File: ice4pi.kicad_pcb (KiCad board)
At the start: 4 copper layers, 85 x 56 mm, 40 parts, among them J1 Conn_02x03, J2 Raspberry_Pi_2_3, J3 USB_C_Receptacle_USB2.0, J4 RJ45_Abracon_ARJP11A-MASA-B-A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, U1 ENC28J60x-SS, U2 DSC1001DE1-025.0000, U3 TPS2375-1

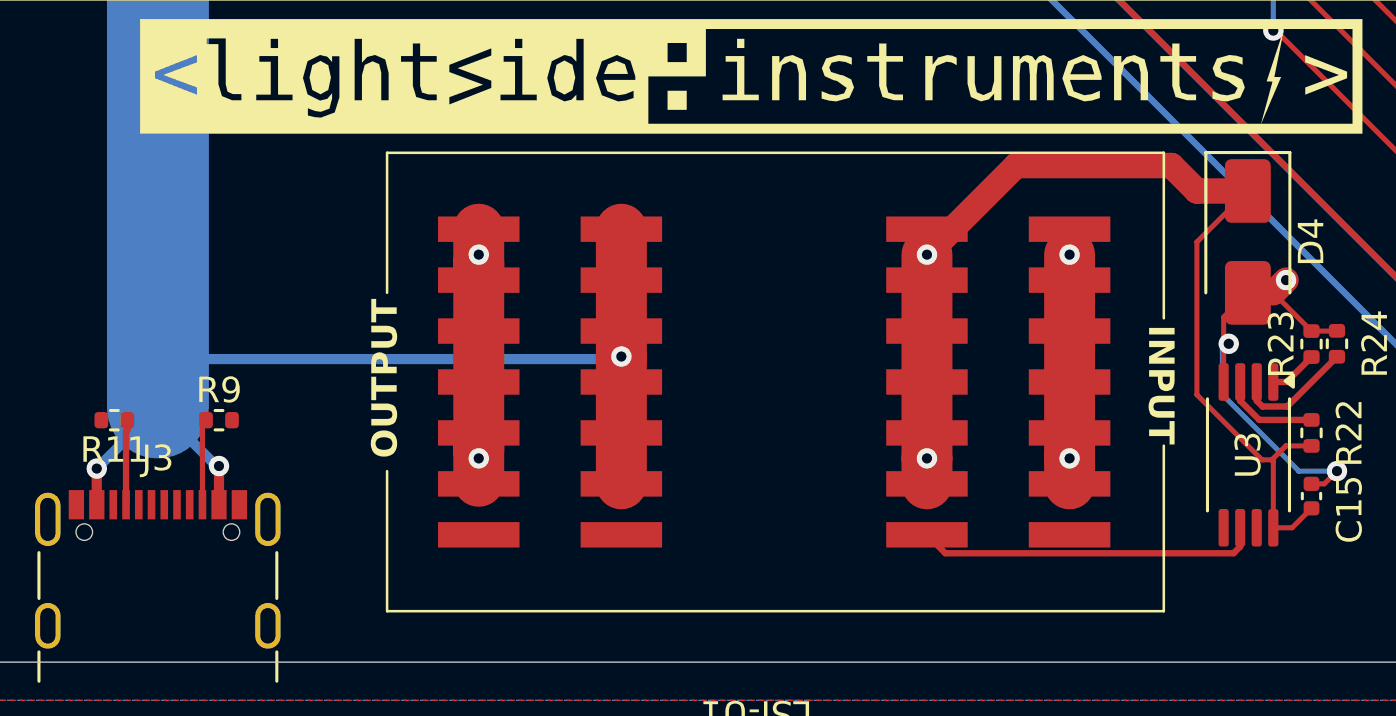
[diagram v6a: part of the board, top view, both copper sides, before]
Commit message: fix: fixed powermod footprint
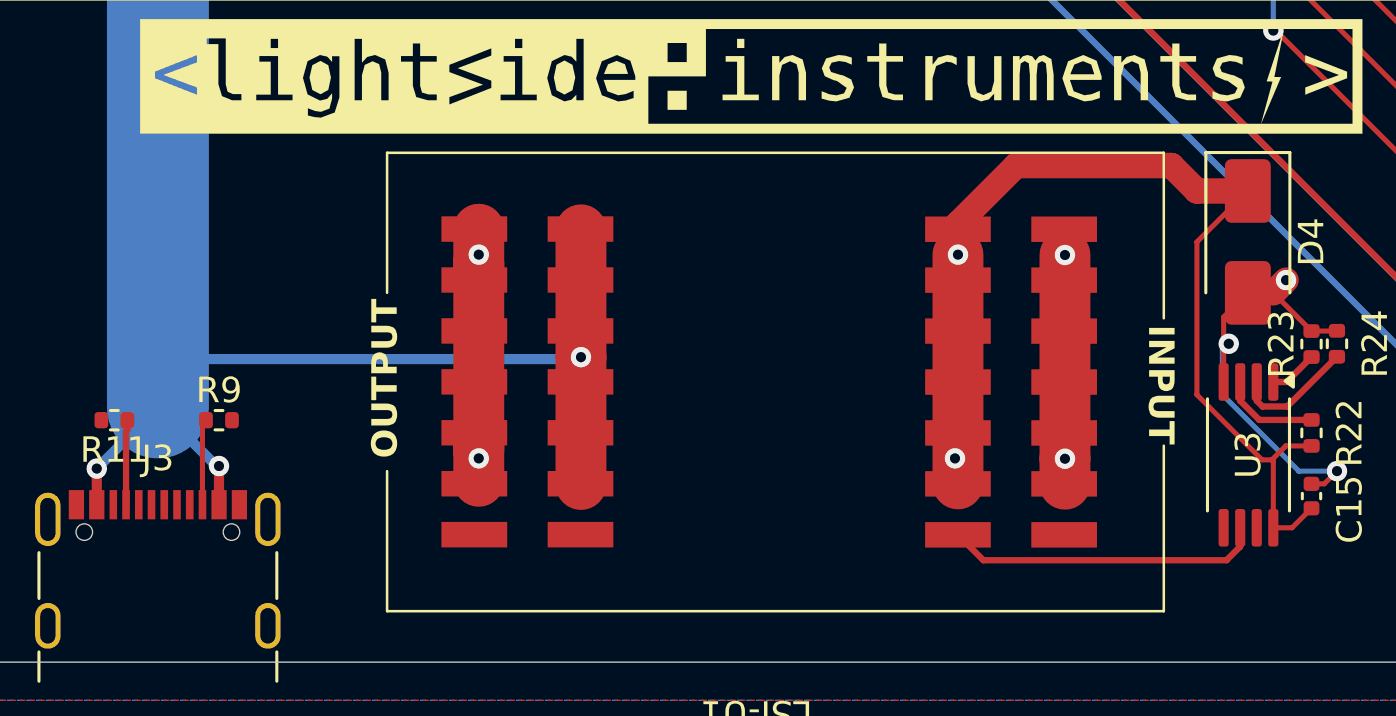
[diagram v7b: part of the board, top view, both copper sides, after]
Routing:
- net +5V: track 94.2 -> 92.6 mm
- net Net-(LSI-U1-S2): track 13.4 -> 12.5 mm
- net POE_V+: track 96.0 -> 95.0 mm

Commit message: fix: no thermal reliefs
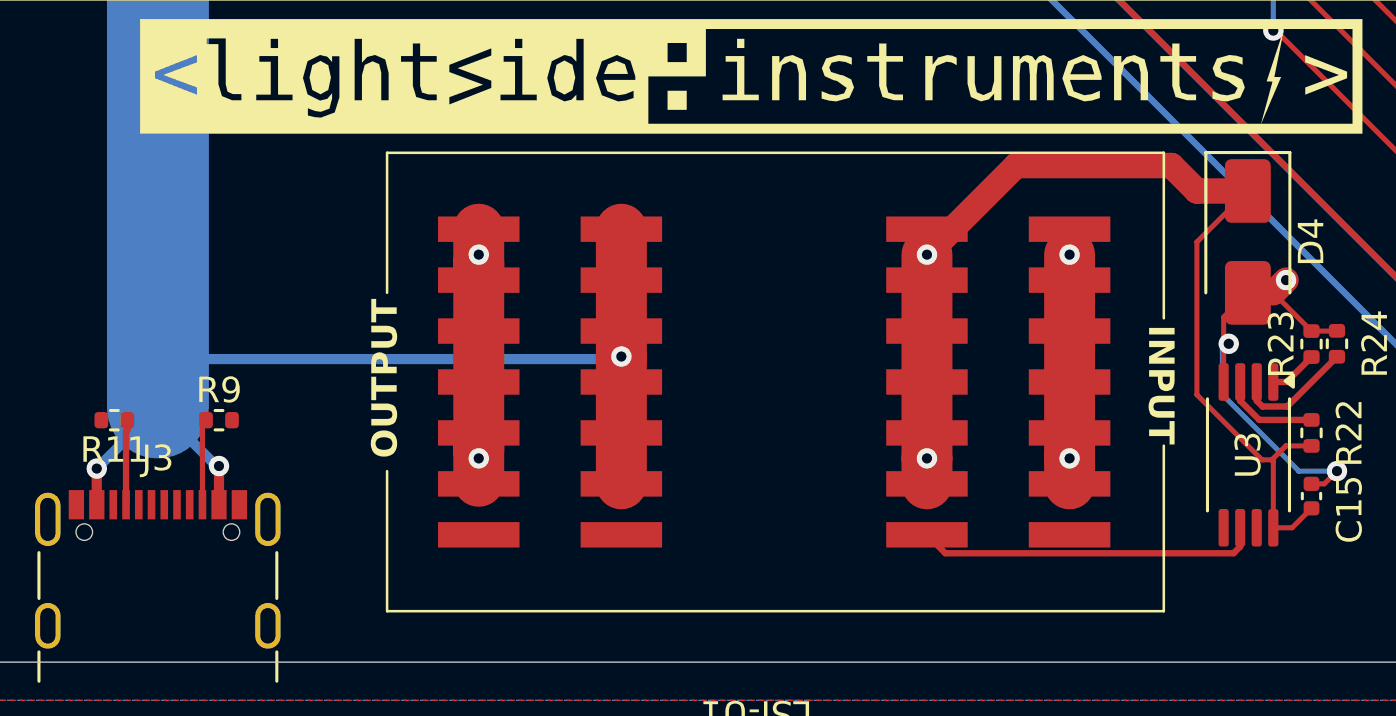
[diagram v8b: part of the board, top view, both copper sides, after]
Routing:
- net +5V: track 92.6 -> 94.2 mm
- net Net-(LSI-U1-S2): track 12.5 -> 13.4 mm
- net POE_V+: track 95.0 -> 96.0 mm
